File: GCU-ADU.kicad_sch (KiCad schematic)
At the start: 5 parts, among them X1 SW_Push, Y1 SW_Push

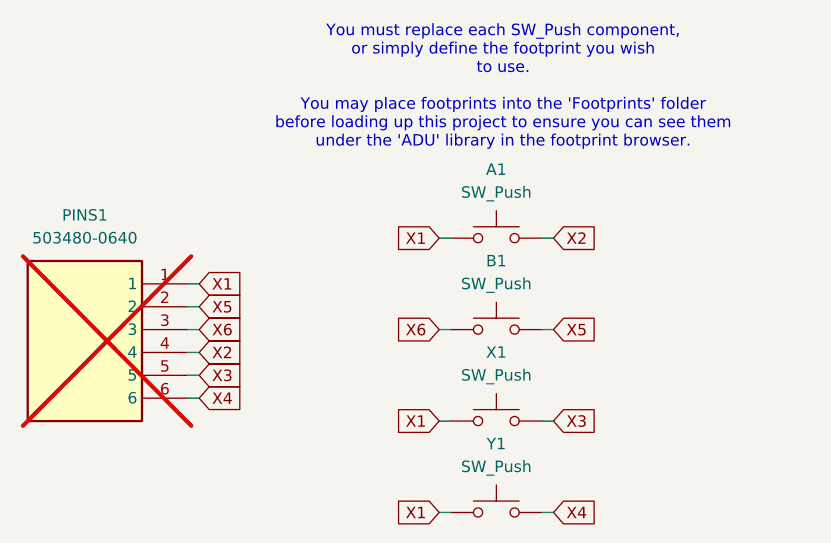
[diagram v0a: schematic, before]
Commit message: Resolve backwards connector pins
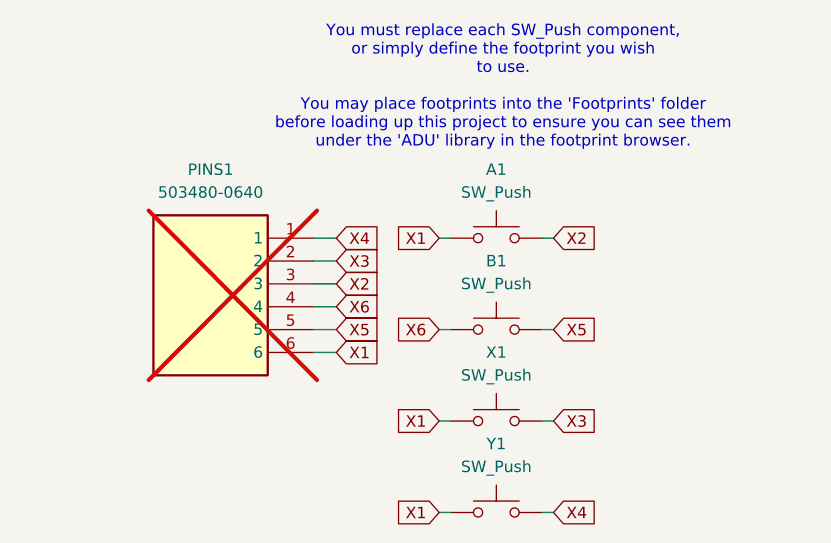
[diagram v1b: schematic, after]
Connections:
- net X1: now also PINS1.6; no longer PINS1.1
- net X2: now also PINS1.3; no longer PINS1.4
- net X3: now also PINS1.2; no longer PINS1.5
- net X4: now also PINS1.1; no longer PINS1.6
- net X5: now also PINS1.5; no longer PINS1.2
- net X6: now also PINS1.4; no longer PINS1.3
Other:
- moved on the sheet: PINS1
